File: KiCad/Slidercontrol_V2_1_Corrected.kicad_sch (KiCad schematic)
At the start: 12 parts, among them J1 Jack-DC, J2 AudioJack3, J3 AudioPlug3, J4 N3 Canon Camera Connector, M1 Stepper_Motor_bipolar, U1 4N33, U3 HC_SR04 Ultrasonic Sensor, u2 Displaymodule, TFT-LCD-Displa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

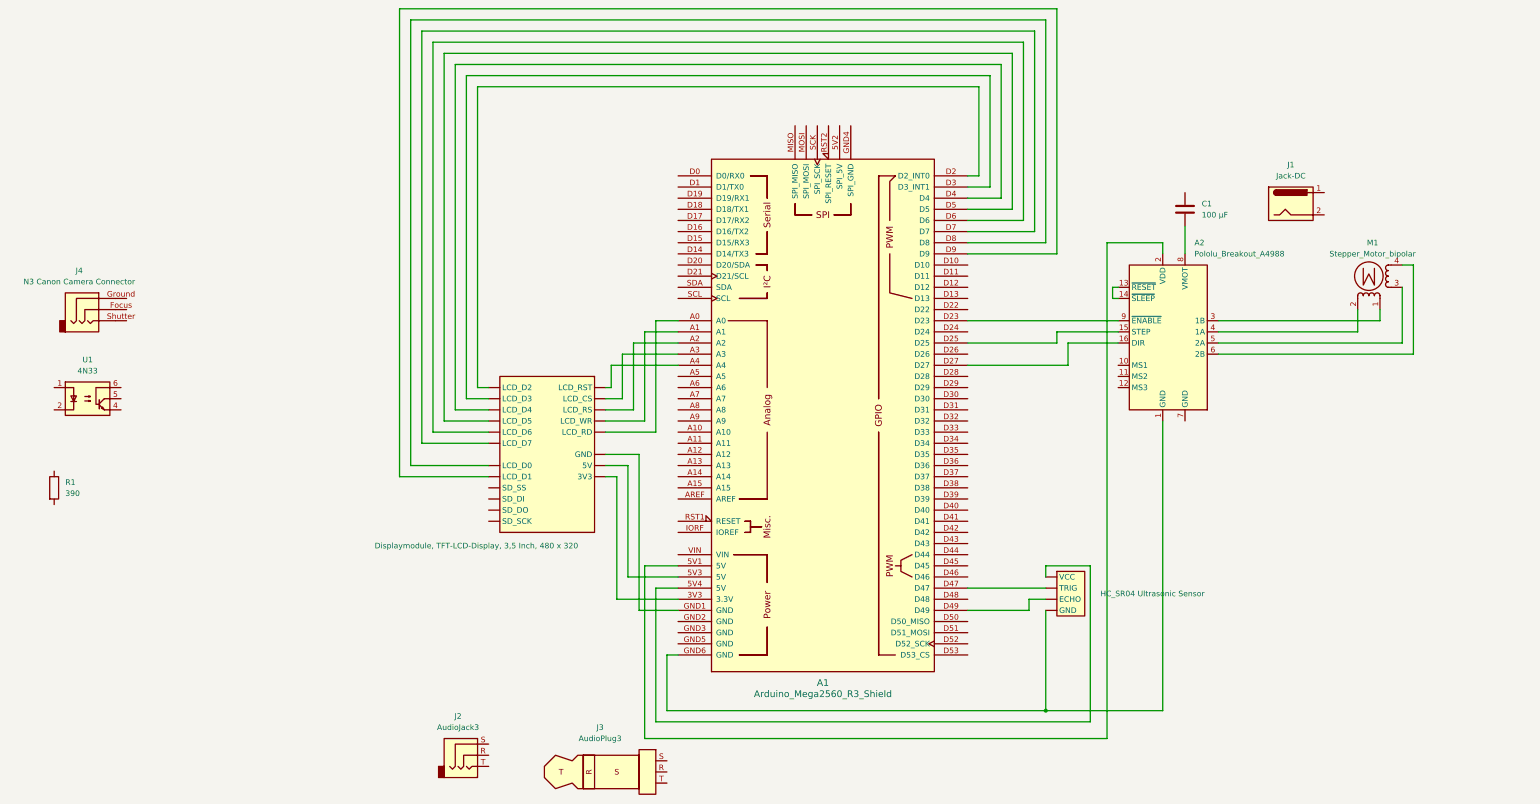
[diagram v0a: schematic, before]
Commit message: Added Schematic
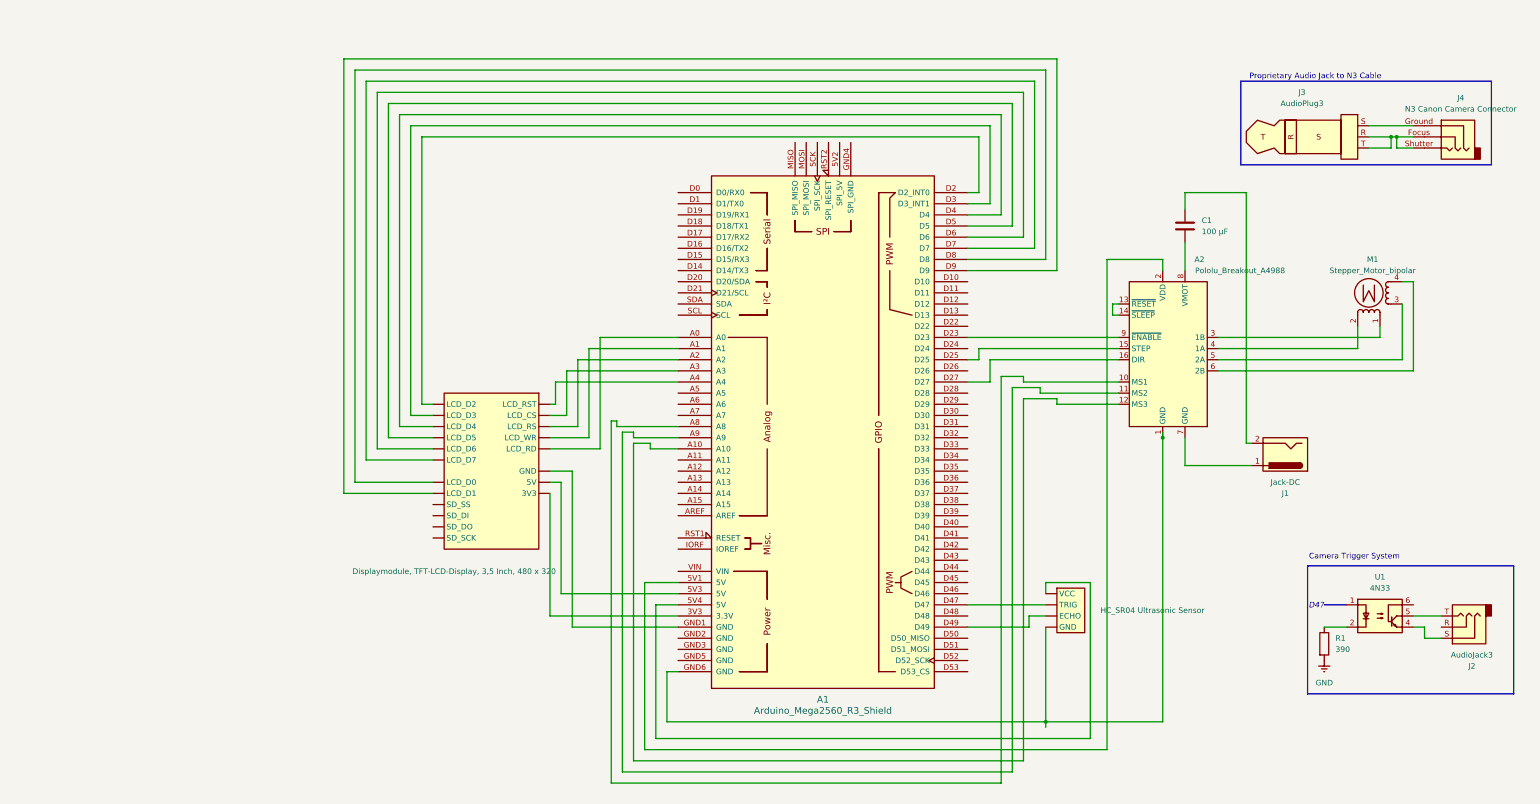
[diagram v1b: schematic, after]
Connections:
- net at J4.Focus: now also J3.R, J3.T, J4.Shutter
- net at J4.Ground: now also J3.S
- net at u2. (SD_SCK): now also A1.GND1 (GND)
- net at J1.1: now also A2.7 (GND)
- net at J1.2: now also C1.1
- net at A1.A10: now also A2.12 (MS3)
- net at A1.A8: now also A2.10 (MS1)
- net at A1.A9: now also A2.11 (MS2)
- net at J2.S: now also U1.4
- net at J2.T: now also U1.5
- net at R1.1: now also U1.2
- net GND: now reaches R1.2
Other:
- note added: "Camera Trigger System"
- note added: "D47"
- note added: "Proprietary Audio Jack to N3 Cable"
- moved on the sheet: A1, A2, C1, J1, J2, J3, J4, M1, R1, U1
